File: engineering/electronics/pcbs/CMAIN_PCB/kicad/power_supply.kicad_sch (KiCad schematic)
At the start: 24 parts, among them U4 URB4805S-6WR3

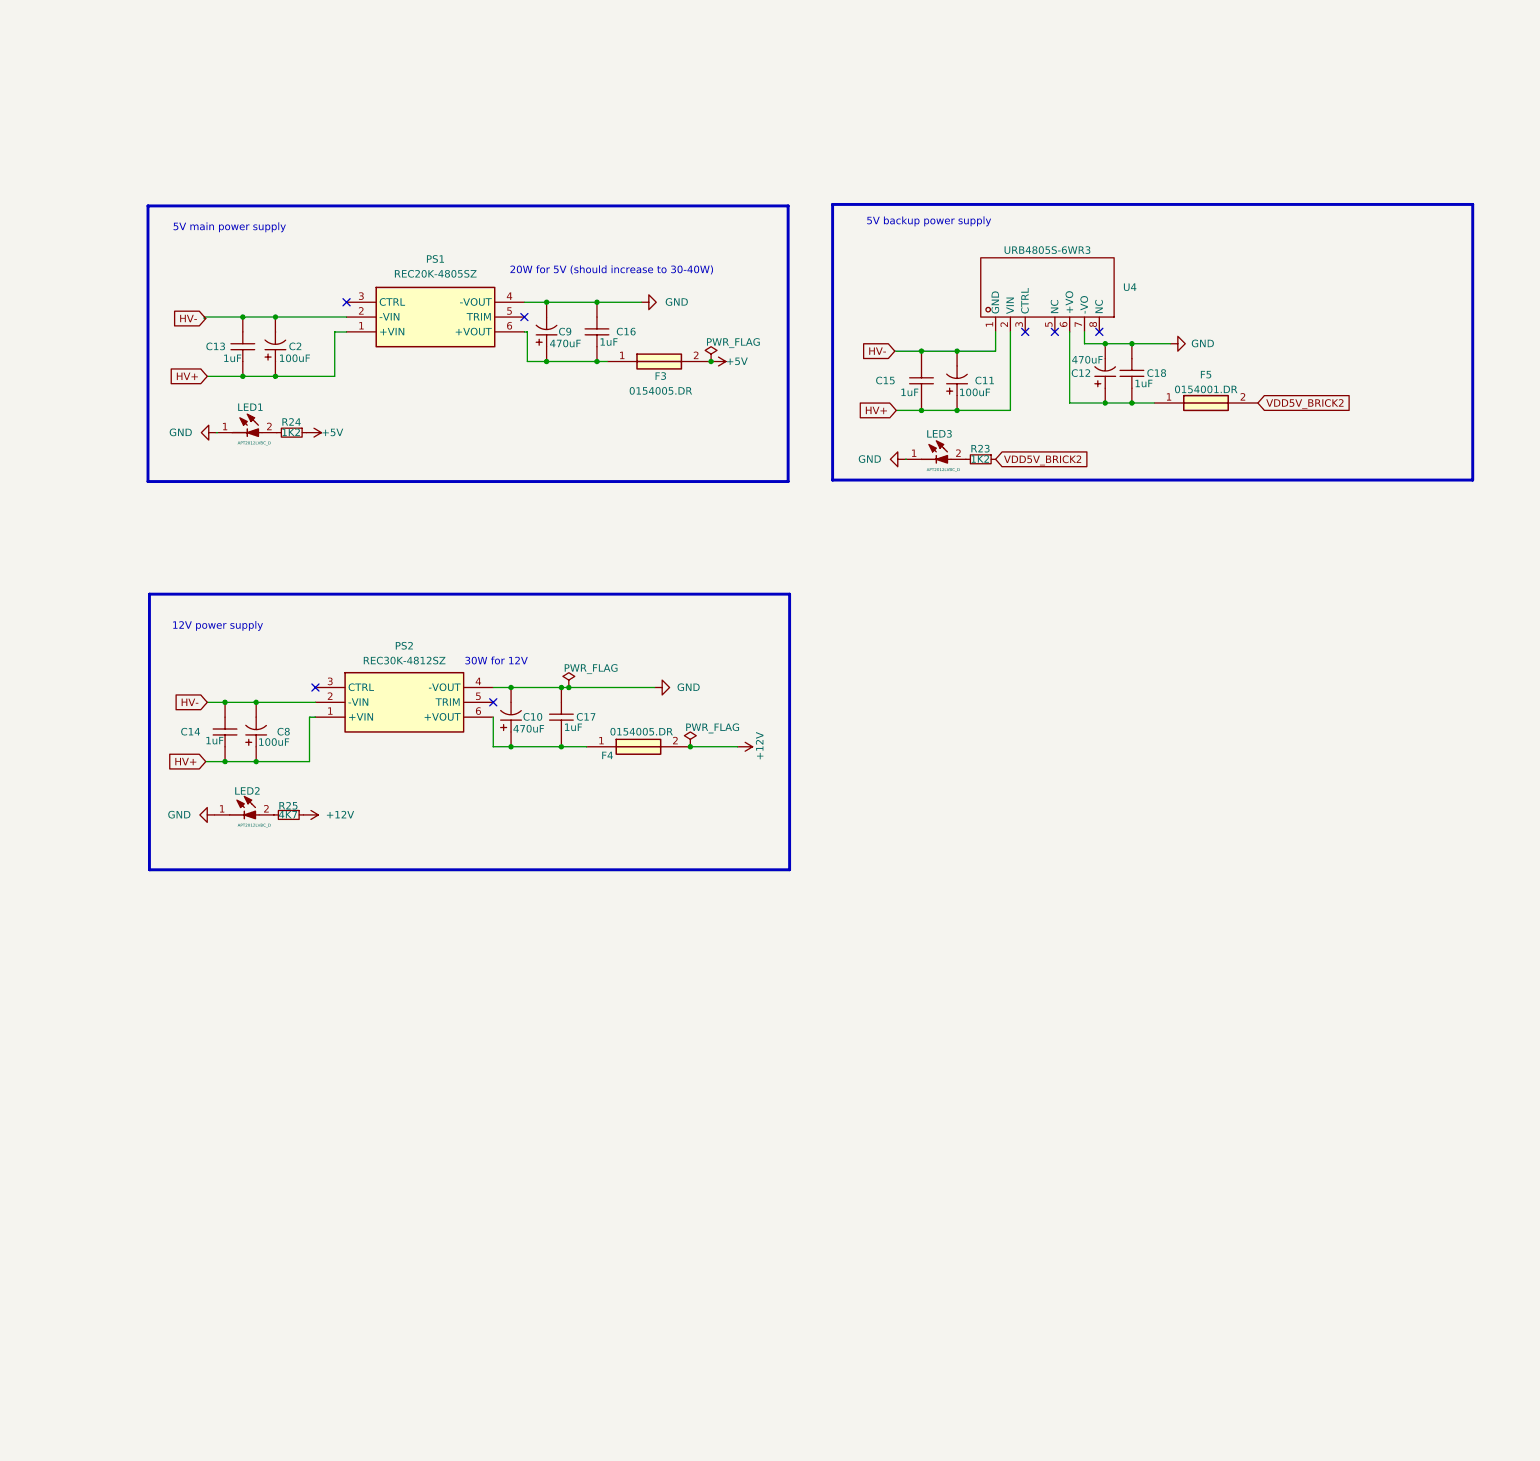
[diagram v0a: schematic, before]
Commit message: Import linked CMAIN PCB layout
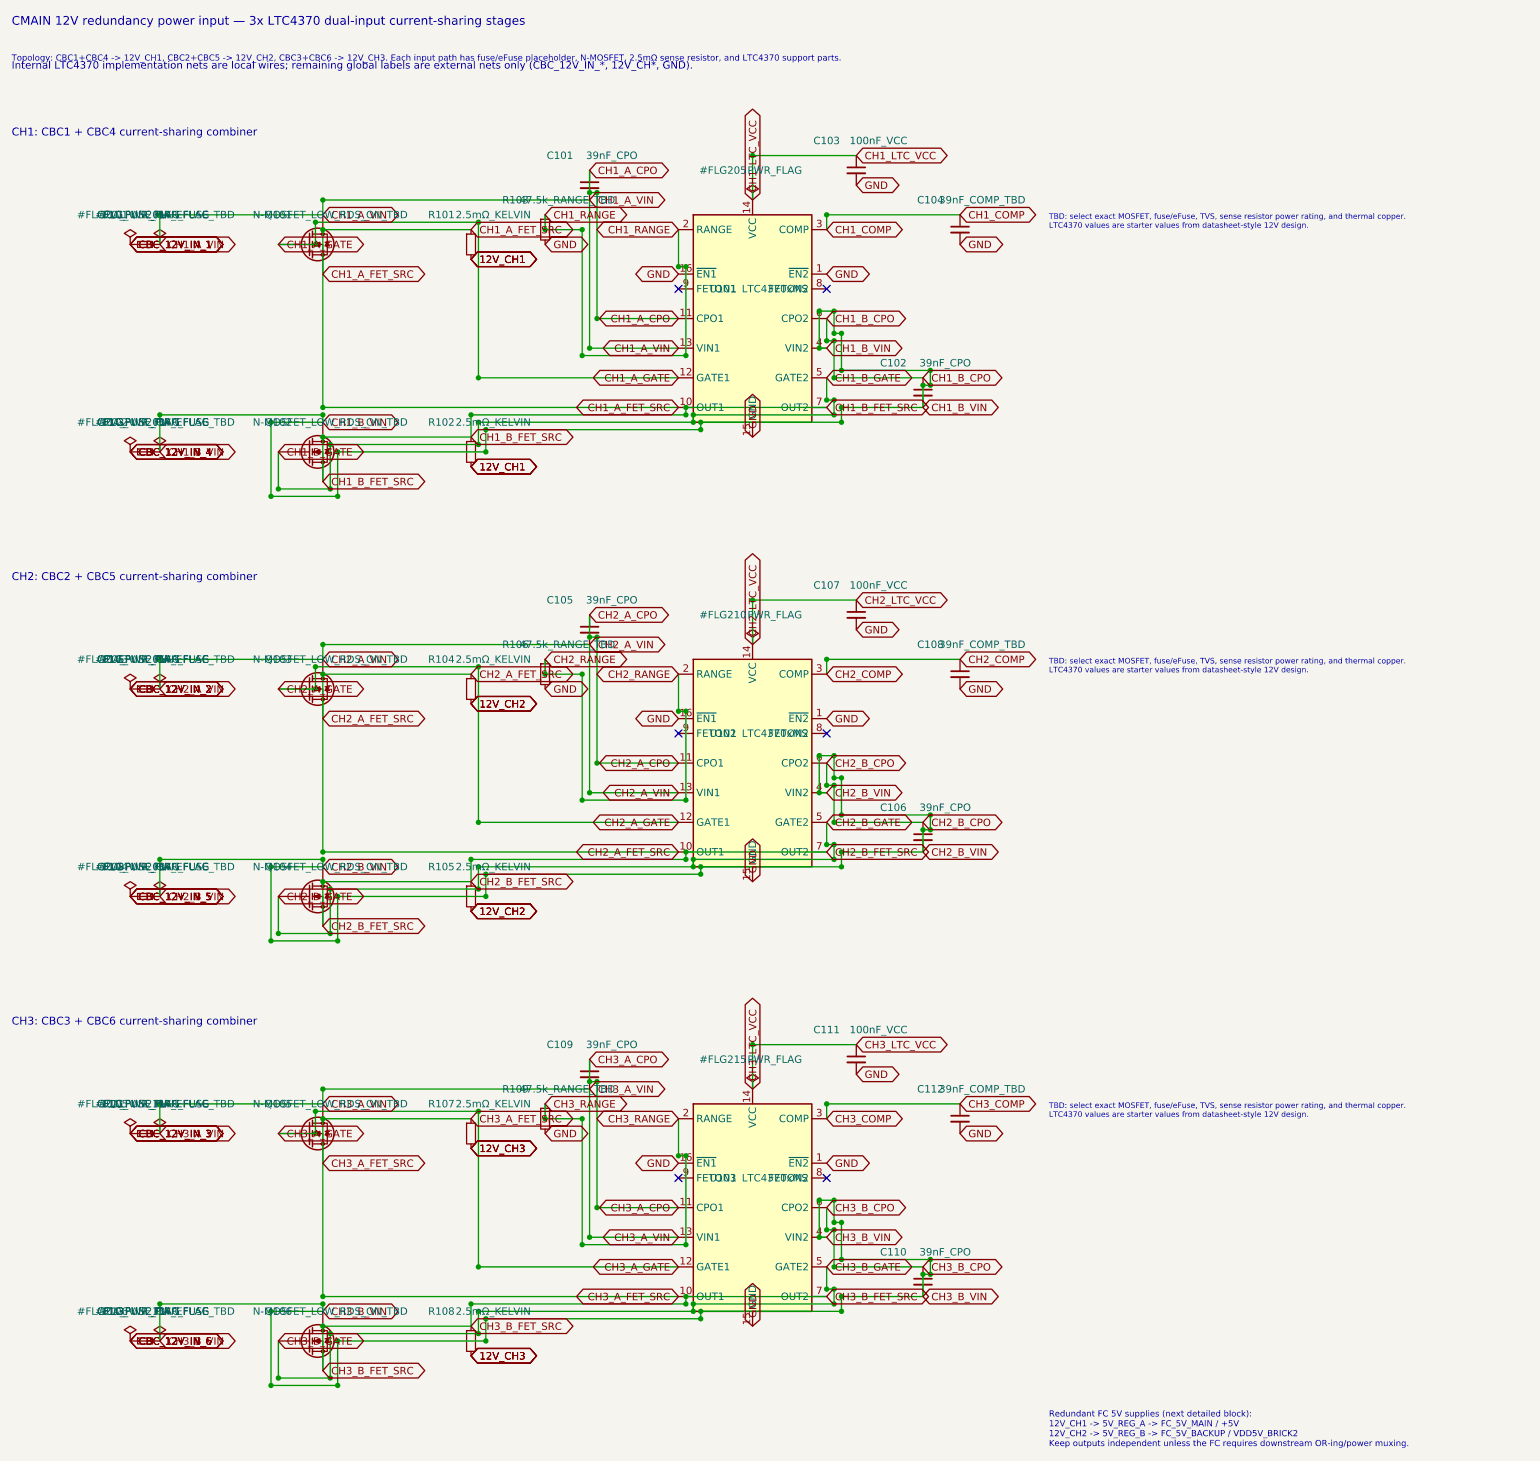
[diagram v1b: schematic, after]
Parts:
- removed C10, C12, C9: 470uF, EasyEDA_Lib:CAP-TH_BD8.0-P3.50-D0.6-FD, symbol Snapeda:SPT1EM471F12OR
- removed C11, C2, C8: 100uF, EasyEDA_Lib:CAP-TH_BD10.0-P5.00-D0.6-FD_2, symbol Snapeda:1011001013R00
- removed C13, C14, C15, C16, C17, C18: 1uF, EasyEDA_Lib:C1206, symbol Snapeda:CL31B105KCHNNNE
- removed F3, F4: 0154005.DR, Samacsys:0154005DR, symbol Samacsys_kicad_sym:0154005.DR
- removed F5: 0154001.DR, Samacsys:0154001DR, symbol Samacsys:0154001.DR
- removed LED1, LED2, LED3: APT2012LVBC_D, Samacsys_kicad_sym:LEDC2012X85N, symbol Samacsys_kicad_sym:APT2012LVBC_D
- removed PS1: REC20K-4805SZ, Samacsys:REC20K, symbol Samacsys_kicad_sym:REC20K-4805SZ
- removed PS2: REC30K-4812SZ, Samacsys:REC30K, symbol Samacsys_kicad_sym:REC30K-4812SZ
- removed R23, R24: 1K2, Resistor_SMD:R_0805_2012Metric_Pad1.20x1.40mm_HandSolder, symbol Device:R_Small
- removed R25: 4K7, Resistor_SMD:R_0805_2012Metric_Pad1.20x1.40mm_HandSolder, symbol Device:R_Small
- removed U4: URB4805S-6WR3, EasyEDA_Lib:PWRM-TH_YLPTEC_URBXXXXS-6WR3, symbol Snapeda:URB4805S-6WR3_C19724400
- added C101, C102, C105, C106, C109, C110: 39nF_CPO, Capacitor_SMD:C_0603_1608Metric, symbol Device:C_Small
- added C103, C107, C111: 100nF_VCC, Capacitor_SMD:C_0603_1608Metric, symbol Device:C_Small
- added C104, C108, C112: 39nF_COMP_TBD, Capacitor_SMD:C_0603_1608Metric, symbol Device:C_Small
- added F101, F102, F103, F104, F105, F106: 10A_FUSE_OR_EFUSE_TBD, symbol Device:Fuse_Small
- added Q101, Q102, Q103, Q104, Q105, Q106: N-MOSFET_LOW_RDS_ON_TBD, symbol Device:Q_NMOS
- added R101, R102, R104, R105, R107, R108: 2.5mΩ_KELVIN, Resistor_SMD:R_2512_6332Metric, symbol Device:R_Small
- added R103, R106, R109: 47.5k_RANGE_TBD, Resistor_SMD:R_0805_2012Metric_Pad1.20x1.40mm_HandSolder, symbol Device:R_Small
- added U101, U102, U103: LTC4370xMS, Package_SO:MSOP-16_3x4.039mm_P0.5mm, symbol Power_Management:LTC4370xMS
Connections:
- net GND: now also C103.2, C104.2, C107.2, C108.2, C111.2, C112.2, R103.2, R106.2, R109.2, U101.1 (~{EN2}), U101.15 (GND), U101.16 (~{EN1}), U102.1 (~{EN2}), U102.15 (GND), U102.16 (~{EN1}), U103.1 (~{EN2}), U103.15 (GND), U103.16 (~{EN1})
- new net 12V_CH1: R101.2, R102.2
- new net 12V_CH2: R104.2, R105.2
- new net 12V_CH3: R107.2, R108.2
- new net CBC_12V_IN_1: F101.1
- new net CBC_12V_IN_2: F103.1
- new net CBC_12V_IN_3: F105.1
- new net CBC_12V_IN_4: F102.1
- new net CBC_12V_IN_5: F104.1
- new net CBC_12V_IN_6: F106.1
- new net CH1_A_CPO: C101.1, U101.11 (CPO1)
- new net CH1_A_FET_SRC: Q101.S, R101.1, U101.10 (OUT1)
- new net CH1_A_GATE: Q101.G, U101.12 (GATE1)
- new net CH1_A_VIN: C101.2, F101.2, Q101.D, U101.13 (VIN1)
- new net CH1_B_CPO: C102.1, U101.6 (CPO2)
- new net CH1_B_FET_SRC: Q102.S, R102.1, U101.7 (OUT2)
- new net CH1_B_GATE: Q102.G, U101.5 (GATE2)
- new net CH1_B_VIN: C102.2, F102.2, Q102.D, U101.4 (VIN2)
- new net CH1_COMP: C104.1, U101.3 (COMP)
- new net CH1_LTC_VCC: C103.1, U101.14 (VCC)
- new net CH1_RANGE: R103.1, U101.2 (RANGE)
- new net CH2_A_CPO: C105.1, U102.11 (CPO1)
- new net CH2_A_FET_SRC: Q103.S, R104.1, U102.10 (OUT1)
- new net CH2_A_GATE: Q103.G, U102.12 (GATE1)
- new net CH2_A_VIN: C105.2, F103.2, Q103.D, U102.13 (VIN1)
- new net CH2_B_CPO: C106.1, U102.6 (CPO2)
- new net CH2_B_FET_SRC: Q104.S, R105.1, U102.7 (OUT2)
- new net CH2_B_GATE: Q104.G, U102.5 (GATE2)
- new net CH2_B_VIN: C106.2, F104.2, Q104.D, U102.4 (VIN2)
- new net CH2_COMP: C108.1, U102.3 (COMP)
- new net CH2_LTC_VCC: C107.1, U102.14 (VCC)
- new net CH2_RANGE: R106.1, U102.2 (RANGE)
- new net CH3_A_CPO: C109.1, U103.11 (CPO1)
- new net CH3_A_FET_SRC: Q105.S, R107.1, U103.10 (OUT1)
- new net CH3_A_GATE: Q105.G, U103.12 (GATE1)
- new net CH3_A_VIN: C109.2, F105.2, Q105.D, U103.13 (VIN1)
- new net CH3_B_CPO: C110.1, U103.6 (CPO2)
- new net CH3_B_FET_SRC: Q106.S, R108.1, U103.7 (OUT2)
- new net CH3_B_GATE: Q106.G, U103.5 (GATE2)
- new net CH3_B_VIN: C110.2, F106.2, Q106.D, U103.4 (VIN2)
- new net CH3_COMP: C112.1, U103.3 (COMP)
- new net CH3_LTC_VCC: C111.1, U103.14 (VCC)
- new net CH3_RANGE: R109.1, U103.2 (RANGE)
- no-connect marks 7 -> 6
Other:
- note added: "CH1: CBC1 + CBC4 current-sharing combiner"
- note added: "CH2: CBC2 + CBC5 current-sharing combiner"
- note added: "CH3: CBC3 + CBC6 current-sharing combiner"
- note added: "CMAIN 12V redundancy power input — 3x LTC4370 dual-input current-sharing stages"
- note added: "Internal LTC4370 implementation nets are local wires; remaining global labels are external nets only (CBC_12V_IN_*, 12V_CH*, GND)."
- note added: "Redundant FC 5V supplies (next detailed block): 12V_CH1 -> 5V_REG_A -> FC_5V_MAIN / +5V 12V_CH2 -> 5V_REG_B -> FC_5V_BACKUP / VDD5V_BRICK2 Keep outputs independent unless the FC requires downstream OR-ing/power muxing."
- note added: "TBD: select exact MOSFET, fuse/eFuse, TVS, sense resistor power rating, and thermal copper. LTC4370 values are starter values from datasheet-style 12V design."
- note added: "Topology: CBC1+CBC4 -> 12V_CH1, CBC2+CBC5 -> 12V_CH2, CBC3+CBC6 -> 12V_CH3. Each input path has fuse/eFuse placeholder, N-MOSFET, 2.5mΩ sense resistor, and LTC4370 support parts."
- note removed: "12V power supply"
- note removed: "20W for 5V (should increase to 30-40W)"
- note removed: "30W for 12V"
- note removed: "5V backup power supply"
- note removed: "5V main power supply"
